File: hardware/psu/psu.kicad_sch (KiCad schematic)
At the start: 58 parts, among them J1 Conn_01x02, J10 Conn_01x04, J11 Conn_01x03, J12 Conn_01x02, J13 Conn_01x03, J14 Conn_01x05, J2 Conn_01x05, J3 Conn_01x02, J4 Conn_01x06, J5 Conn_01x03, J6 Conn_01x05, J7 Conn_01x08, J8 Conn_01x03, J9 Conn_01x04, SW1 SW_SPST, T1 AS-1T175, U1 LM7905_TO220

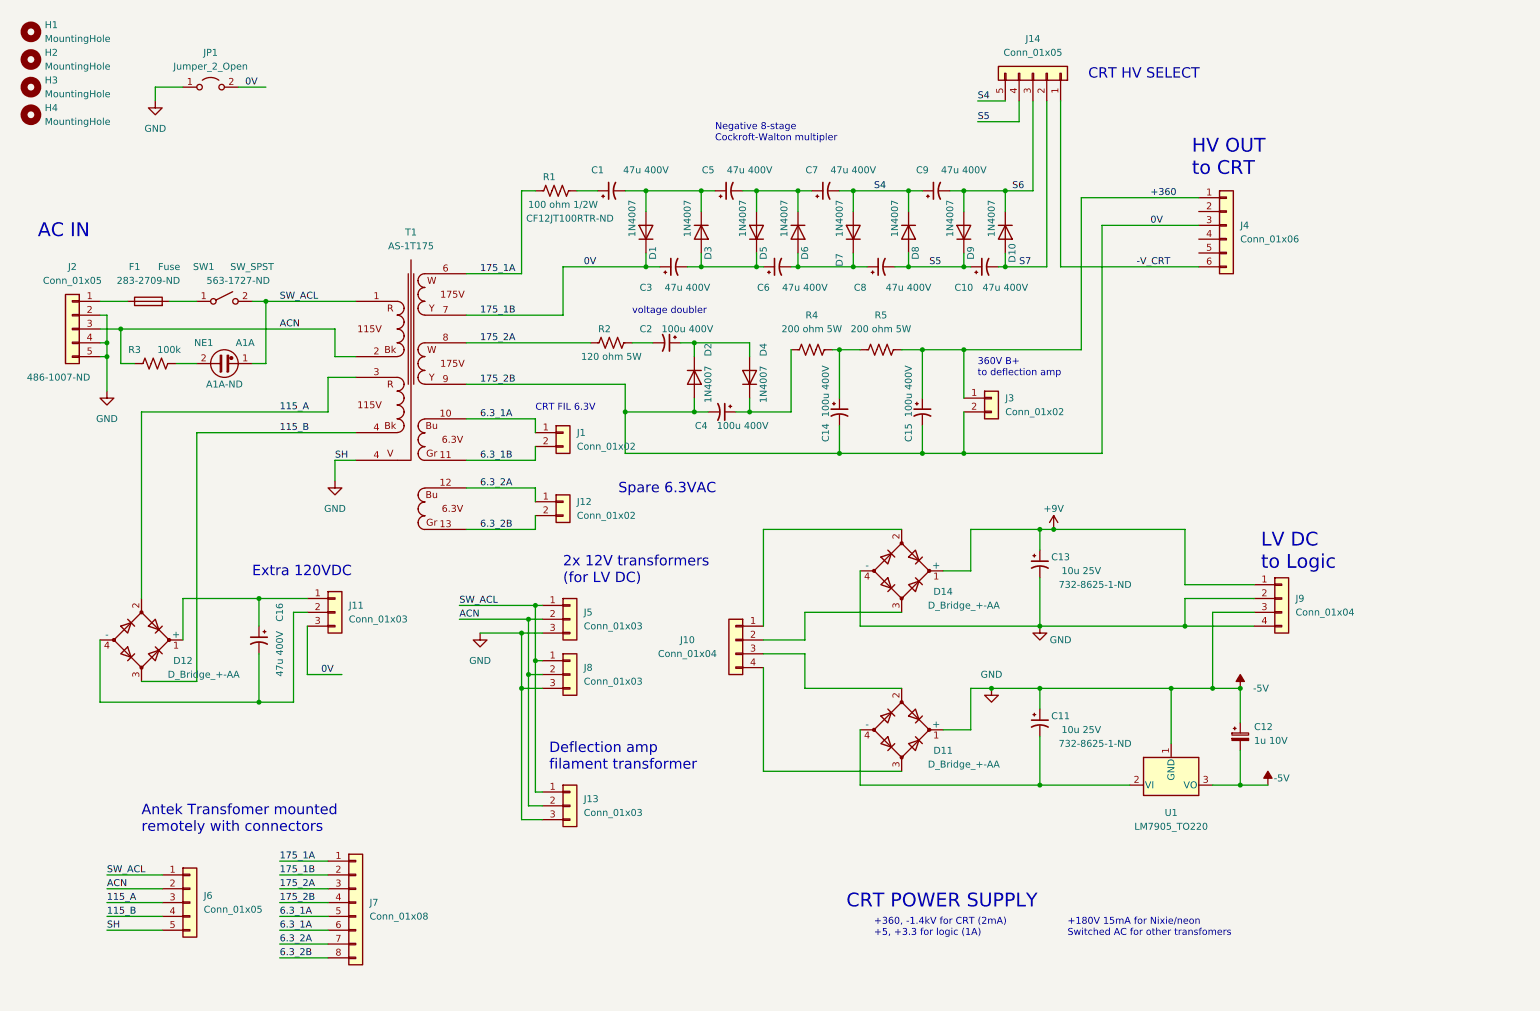
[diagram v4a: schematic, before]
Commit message: Mess with 3D model, clean schematic ERC errors
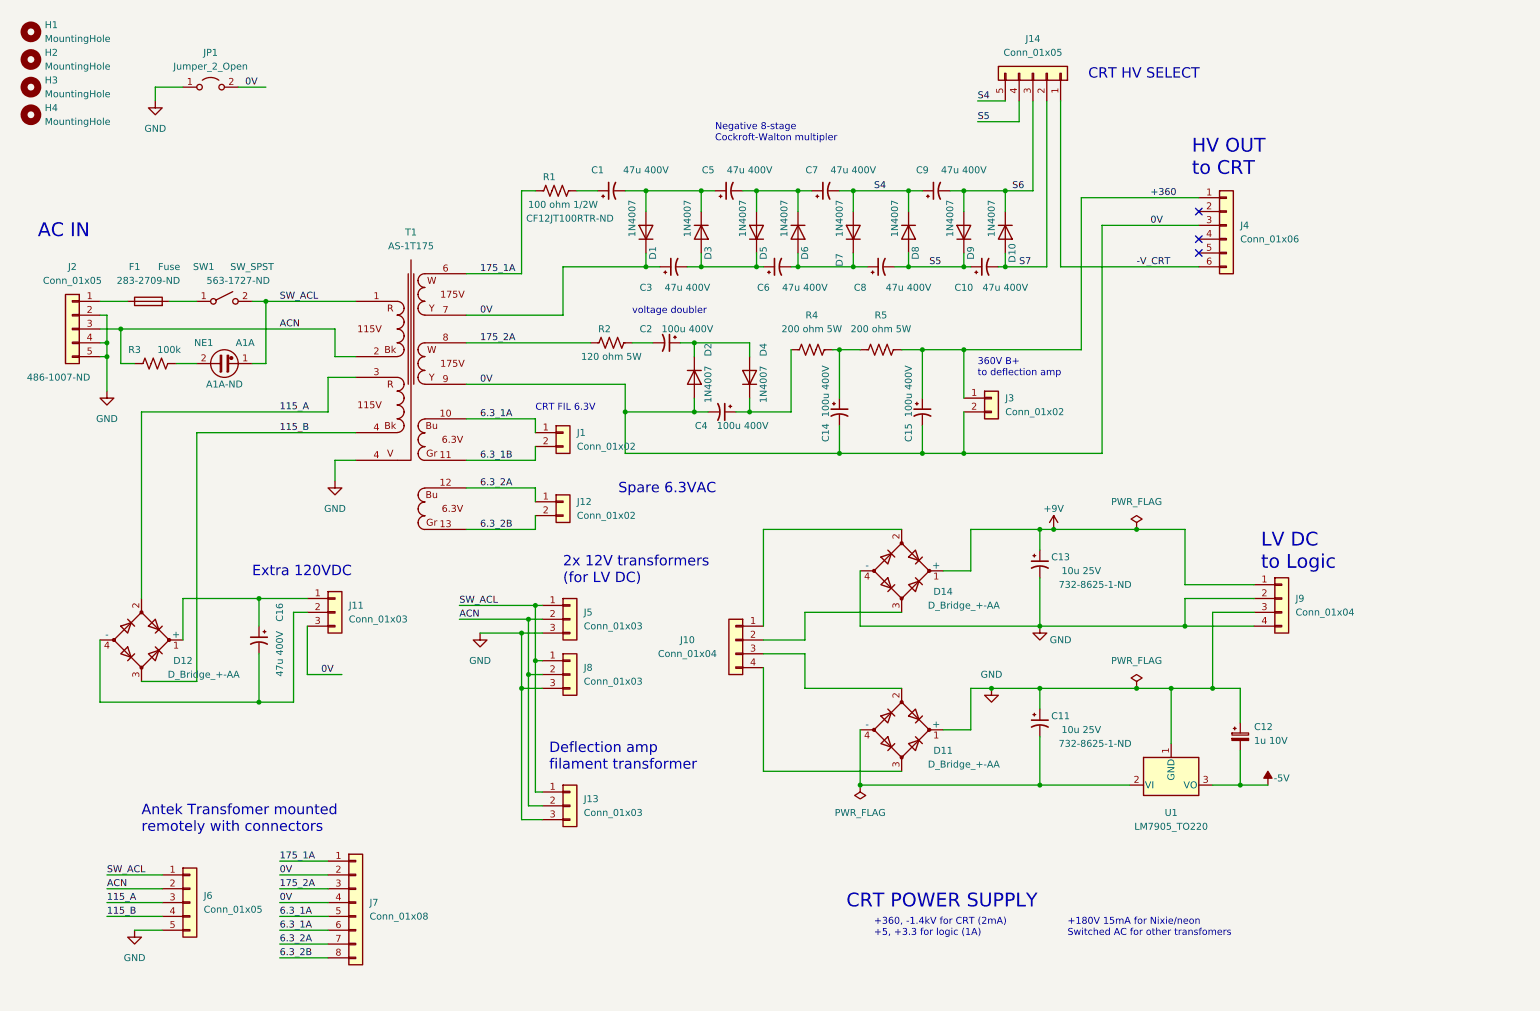
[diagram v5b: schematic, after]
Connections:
- net -5V: no longer C11.1, C12.1, C13.2, D11.1 (+), D14.4 (-), J13.3 (Pin_3), J2.2 (Pin_2), J2.4 (Pin_4), J2.5 (Pin_5), J5.3 (Pin_3), J6.5 (Pin_5), J8.3 (Pin_3), J9.2 (Pin_2), J9.3 (Pin_3), J9.4 (Pin_4), JP1.1 (A), T1.4 (SH), U1.1 (GND)
- new net GND: C11.1, C12.1, C13.2, D11.1 (+), D14.4 (-), J13.3 (Pin_3), J2.2 (Pin_2), J2.4 (Pin_4), J2.5 (Pin_5), J5.3 (Pin_3), J6.5 (Pin_5), J8.3 (Pin_3), J9.2 (Pin_2), J9.3 (Pin_3), J9.4 (Pin_4), JP1.1 (A), T1.4 (SH), U1.1 (GND)
- no-connect marks 0 -> 3
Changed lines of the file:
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@@
   (junction (at 138.43 45.72) (diameter 0) (color 0 0 0 0)
   )
-  (junction (at 237.49 137.16) (diameter 0) (color 0 0 0 0)
-  )
   (junction (at 107.95 132.08) (diameter 0) (color 0 0 0 0)
   )
@@
   (junction (at 200.66 137.16) (diameter 0) (color 0 0 0 0)
   )
+  (junction (at 218.44 137.16) (diameter 0) (color 0 0 0 0)
+  )
   (junction (at 58.42 66.04) (diameter 0) (color 0 0 0 0)
   )
@@
   (junction (at 232.41 137.16) (diameter 0) (color 0 0 0 0)
   )
+  (junction (at 167.64 154.94) (diameter 0) (color 0 0 0 0)
+  )
   (junction (at 200.66 125.73) (diameter 0) (color 0 0 0 0)
   )
@@
   (junction (at 156.21 45.72) (diameter 0) (color 0 0 0 0)
   )
+  (junction (at 218.44 107.95) (diameter 0) (color 0 0 0 0)
+  )
   (junction (at 166.37 59.69) (diameter 0) (color 0 0 0 0)
   )
@@
   (junction (at 105.41 127) (diameter 0) (color 0 0 0 0)
   )
+  (no_connect (at 229.87 57.15))
+  (no_connect (at 229.87 54.61))
+  (no_connect (at 229.87 49.53))
   (wire (pts (xy 200.66 107.95) (xy 203.2 107.95))
     (stroke (width 0) (type default) (color 0 0 0 0))
@@
     (stroke (width 0) (type default) (color 0 0 0 0))
   )
+  (wire (pts (xy 218.44 107.95) (xy 203.2 107.95))
+    (stroke (width 0) (type default) (color 0 0 0 0))
+  )
   (wire (pts (xy 95.25 68.58) (xy 113.03 68.58))
     (stroke (width 0) (type default) (color 0 0 0 0))
@@
     (stroke (width 0) (type default) (color 0 0 0 0))
   )
-  (wire (pts (xy 227.33 107.95) (xy 203.2 107.95))
+  (wire (pts (xy 227.33 107.95) (xy 218.44 107.95))
     (stroke (width 0) (type default) (color 0 0 0 0))
   )
@@
     (stroke (width 0) (type default) (color 0 0 0 0))
   )
-  (wire (pts (xy 200.66 137.16) (xy 224.79 137.16))
+  (wire (pts (xy 200.66 137.16) (xy 218.44 137.16))
     (stroke (width 0) (type default) (color 0 0 0 0))
   )
@@
     (stroke (width 0) (type default) (color 0 0 0 0))
   )
+  (wire (pts (xy 218.44 137.16) (xy 224.79 137.16))
+    (stroke (width 0) (type default) (color 0 0 0 0))
+  )
   (wire (pts (xy 186.69 74.93) (xy 208.28 74.93))
     (stroke (width 0) (type default) (color 0 0 0 0))
@@
     (stroke (width 0) (type default) (color 0 0 0 0))
   )
-  (wire (pts (xy 29.21 181.61) (xy 39.37 181.61))
-    (stroke (width 0) (type default) (color 0 0 0 0))
-  )
   (wire (pts (xy 95.25 95.25) (xy 107.95 95.25))
     (stroke (width 0) (type default) (color 0 0 0 0))
@@
   )
   (wire (pts (xy 106.68 134.62) (xy 106.68 124.46))
+    (stroke (width 0) (type default) (color 0 0 0 0))
+  )
+  (wire (pts (xy 34.29 181.61) (xy 39.37 181.61))
     (stroke (width 0) (type default) (color 0 0 0 0))
   )
@@
     (effects (font (size 1.27 1.27)) (justify left bottom))
   )
-  (label "SH" (at 71.12 95.25 0)
-    (effects (font (size 1.27 1.27)) (justify left bottom))
-  )
   (label "6.3_1B" (at 97.79 95.25 0)
     (effects (font (size 1.27 1.27)) (justify left bottom))
@@
     (effects (font (size 1.27 1.27)) (justify left bottom))
   )
-  (label "175_1B" (at 60.96 171.45 0)
+  (label "0V" (at 60.96 171.45 0)
     (effects (font (size 1.27 1.27)) (justify left bottom))
   )
@@
     (effects (font (size 1.27 1.27)) (justify left bottom))
   )
+  (label "0V" (at 97.79 81.28 0)
+    (effects (font (size 1.27 1.27)) (justify left bottom))
+  )
   (label "115_A" (at 60.96 86.36 0)
     (effects (font (size 1.27 1.27)) (justify left bottom))
   )
-  (label "175_2B" (at 97.79 81.28 0)
-    (effects (font (size 1.27 1.27)) (justify left bottom))
-  )
   (label "0V" (at 220.98 52.07 0)
     (effects (font (size 1.27 1.27)) (justify left bottom))
@@
     (effects (font (size 1.27 1.27)) (justify left bottom))
   )
-  (label "SH" (at 29.21 181.61 0)
-    (effects (font (size 1.27 1.27)) (justify left bottom))
-  )
   (label "115_A" (at 29.21 176.53 0)
     (effects (font (size 1.27 1.27)) (justify left bottom))
   )
-  (label "175_1B" (at 97.79 68.58 0)
-    (effects (font (size 1.27 1.27)) (justify left bottom))
-  )
   (label "S4" (at 170.18 45.72 0)
     (effects (font (size 1.27 1.27)) (justify left bottom))
@@
     (effects (font (size 1.27 1.27)) (justify left bottom))
   )
-  (label "175_2B" (at 60.96 176.53 0)
+  (label "0V" (at 60.96 176.53 0)
     (effects (font (size 1.27 1.27)) (justify left bottom))
   )
@@
     (effects (font (size 1.27 1.27)) (justify left bottom))
   )
-  (label "0V" (at 116.84 59.69 0)
+  (label "0V" (at 97.79 68.58 0)
     (effects (font (size 1.27 1.27)) (justify left bottom))
   )
@@
     (pin "1")
   )
-  (symbol (lib_id "power:-5V") (at 237.49 137.16 0) (unit 1)
-    (in_bom yes) (on_board yes)
-    (property "Reference" "#PWR08" (id 0) (at 237.49 134.62 0)
-      (effects (font (size 1.27 1.27)) hide)
-    )
-    (property "Value" "-5V" (id 1) (at 241.3 137.16 0))
-    (property "Footprint" "" (id 2) (at 237.49 137.16 0)
-      (effects (font (size 1.27 1.27)) hide)
-    )
-    (property "Datasheet" "" (id 3) (at 237.49 137.16 0)
-      (effects (font (size 1.27 1.27)) hide)
-    )
-    (pin "1")
-  )
   (symbol (lib_id "Device:D_Bridge_+AA-") (at 175.26 144.78 0) (unit 1)
     (in_bom yes) (on_board yes)
@@
     (pin "3")
     (pin "4")
+  )
+  (symbol (lib_id "power:PWR_FLAG") (at 218.44 107.95 0) (unit 1)
+    (in_bom yes) (on_board yes) (fields_autoplaced)
+    (property "Reference" "#FLG0102" (id 0) (at 218.44 106.045 0)
+      (effects (font (size 1.27 1.27)) hide)
+    )
+    (property "Value" "PWR_FLAG" (id 1) (at 218.44 102.87 0))
+    (property "Footprint" "" (id 2) (at 218.44 107.95 0)
+      (effects (font (size 1.27 1.27)) hide)
+    )
+    (property "Datasheet" "~" (id 3) (at 218.44 107.95 0)
+      (effects (font (size 1.27 1.27)) hide)
+    )
+    (pin "1")
   )
   (symbol (lib_id "Connector_Generic:Conn_01x03") (at 114.3 134.62 0) (unit 1)
@@
     (pin "1")
   )
+  (symbol (lib_id "power:PWR_FLAG") (at 167.64 154.94 180) (unit 1)
+    (in_bom yes) (on_board yes) (fields_autoplaced)
+    (property "Reference" "#FLG0101" (id 0) (at 167.64 156.845 0)
+      (effects (font (size 1.27 1.27)) hide)
+    )
+    (property "Value" "PWR_FLAG" (id 1) (at 167.64 160.02 0))
+    (property "Footprint" "" (id 2) (at 167.64 154.94 0)
+      (effects (font (size 1.27 1.27)) hide)
+    )
+    (property "Datasheet" "~" (id 3) (at 167.64 154.94 0)
+      (effects (font (size 1.27 1.27)) hide)
+    )
+    (pin "1")
+  )
   (symbol (lib_id "Mechanical:MountingHole") (at 15.24 21.59 0) (unit 1)
     (in_bom yes) (on_board yes) (fields_autoplaced)
@@
     (pin "2")
   )
+  (symbol (lib_id "power:GND") (at 34.29 181.61 0) (unit 1)
+    (in_bom yes) (on_board yes) (fields_autoplaced)
+    (property "Reference" "#PWR0101" (id 0) (at 34.29 187.96 0)
+      (effects (font (size 1.27 1.27)) hide)
+    )
+    (property "Value" "GND" (id 1) (at 34.29 186.69 0))
+    (property "Footprint" "" (id 2) (at 34.29 181.61 0)
+      (effects (font (size 1.27 1.27)) hide)
+    )
+    (property "Datasheet" "" (id 3) (at 34.29 181.61 0)
+      (effects (font (size 1.27 1.27)) hide)
+    )
+    (pin "1")
+  )
   (symbol (lib_id "Device:C_Polarized_Small_US") (at 133.35 59.69 90) (unit 1)
     (in_bom yes) (on_board yes)
@@
     (pin "2")
   )
+  (symbol (lib_id "power:PWR_FLAG") (at 218.44 137.16 0) (unit 1)
+    (in_bom yes) (on_board yes) (fields_autoplaced)
+    (property "Reference" "#FLG0103" (id 0) (at 218.44 135.255 0)
+      (effects (font (size 1.27 1.27)) hide)
+    )
+    (property "Value" "PWR_FLAG" (id 1) (at 218.44 132.08 0))
+    (property "Footprint" "" (id 2) (at 218.44 137.16 0)
+      (effects (font (size 1.27 1.27)) hide)
+    )
+    (property "Datasheet" "~" (id 3) (at 218.44 137.16 0)
+      (effects (font (size 1.27 1.27)) hide)
+    )
+    (pin "1")
+  )
   (symbol (lib_id "Connector_Generic:Conn_01x05") (at 22.86 71.12 0) (mirror y) (unit 1)
     (in_bom yes) (on_board yes)
@@
   )
   (symbol_instances
+    (path "/7c0b2a49-6be3-4836-a134-d8bdbe2029f9"
+      (reference "#FLG0101") (unit 1) (value "PWR_FLAG") (footprint "")
+    )
+    (path "/6ed3655f-29bb-4a2c-8d53-7428c9d0c253"
+      (reference "#FLG0102") (unit 1) (value "PWR_FLAG") (footprint "")
+    )
+    (path "/e589d2a9-ad10-4803-b8dd-58cae92a0830"
+      (reference "#FLG0103") (unit 1) (value "PWR_FLAG") (footprint "")
+    )
     (path "/441877be-212e-4074-8b8d-3abad024027d"
       (reference "#PWR01") (unit 1) (value "GND") (footprint "")
@@
       (reference "#PWR07") (unit 1) (value "+9V") (footprint "")
     )
-    (path "/374684e0-799b-470a-97c1-5ced756bc232"
-      (reference "#PWR08") (unit 1) (value "-5V") (footprint "")
-    )
     (path "/77c041aa-5845-4c96-9371-bd0f80924889"
       (reference "#PWR09") (unit 1) (value "-5V") (footprint "")
     )
+    (path "/8ead9981-91bb-4421-96ed-723a403729f1"
+      (reference "#PWR0101") (unit 1) (value "GND") (footprint "")
+    )
     (path "/59ac5de6-0fe9-487e-9a5e-3c9d13998e39"

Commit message: working on PSU
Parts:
- added J15: Conn_01x02, Connector_PinHeader_2.54mm:PinHeader_1x02_P2.54mm_Vertical, symbol Connector_Generic:Conn_01x02
- added K1: PR16-12V-540-2C, Package_DIP:DIP-22_W7.62mm_LongPads, symbol my_relay:PR16-12V-540-2A
- added Q1: Q_NMOS_GDS, Package_TO_SOT_THT:TO-220-3_Vertical, symbol Device:Q_NMOS_GDS
- added R10, R11, R6, R7, R8, R9: 1.0M 2W, Resistor_THT:R_Axial_DIN0309_L9.0mm_D3.2mm_P15.24mm_Horizontal, symbol Device:R_US
- added U2, U3: BOM_item, symbol misc_bom:BOM_item
- C1, C10, C16, C3, C5, C6, C7, C8, C9: footprint Capacitor_THT:CP_Radial_D13.0mm_P7.50mm -> Capacitor_THT:CP_Radial_D12.5mm_P5.00mm; CatNo (none) -> 565-EKXJ401ELL470MK30S-ND
- C12: footprint Capacitor_THT:CP_Radial_D5.0mm_P2.00mm -> Capacitor_THT:C_Disc_D5.0mm_W2.5mm_P5.00mm; CatNo (none) -> 445-FK28X5R1A105K-ND
- C14, C15, C2, C4: CatNo (none) -> 493-2567-ND
- JP1: value Jumper_2_Open -> WIRE_JUMPER
- R2: footprint Resistor_THT:R_Axial_Power_L25.0mm_W6.4mm_P27.94mm -> Resistor_THT:R_Axial_DIN0617_L17.0mm_D6.0mm_P25.40mm_Horizontal; CatNo (none) -> A142778CT-ND
- R4, R5: footprint Resistor_THT:R_Axial_Power_L25.0mm_W6.4mm_P27.94mm -> Resistor_THT:R_Axial_DIN0617_L17.0mm_D6.0mm_P25.40mm_Horizontal; CatNo (none) -> A142783CT-ND
- U1: CatNo (none) -> LM7905CTNS/NOPB-ND
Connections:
- net 0V: now also R10.1, R11.1, R7.1
- net 175_1A: now also K1.14; no longer T1.6 (H1A)
- net 175_2A: now also K1.9; no longer T1.8 (H2A)
- net GND: now also J15.2 (Pin_2), Q1.3 (S)
- net S7: now also R9.2
- net at C1.2, C5.1, D1.2 (A)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: now also R6.2
- net at C1.1, R1.2: now also R6.1
- net +9V renamed +12V
- net +12V: now also K1.22
- new net: K1.1, Q1.2 (D)
- new net: K1.11, T1.8 (H2A)
- new net: K1.12, T1.6 (H1A)
- new net: K1.16, R11.2
- new net: K1.7, R10.2
- new net: R7.2, R8.1
- new net: J15.1 (Pin_1), Q1.1 (G)
- new net: R8.2, R9.1
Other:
- note added: "(Maybe usable for +5V)"
- note added: "+180V 15mA for Nixie/neon Switched AC for other transformers"
- note added: "5mm 24 pin breakaway header"
- note added: "HV Enable (logic)"
- note added: "Octal Socket"
- note removed: "+180V 15mA for Nixie/neon Switched AC for other transfomers"
- moved on the sheet: C1, C10, C11, C12, C13, C14, C15, C2, C3, C4, C5, C6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

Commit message: PSU layout done?
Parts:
- removed C16: 47u 400V, Capacitor_THT:CP_Radial_D12.5mm_P5.00mm, symbol Device:C_Polarized_Small_US
- removed D12: D_Bridge_+-AA, Diode_THT:Diode_Bridge_19.0x3.5x10.0mm_P5.0mm, symbol Device:D_Bridge_+AA-
- removed J11: Conn_01x03, Connector_Molex:Molex_KK-396_A-41791-0003_1x03_P3.96mm_Vertical, symbol Connector_Generic:Conn_01x03
- removed JP1: WIRE_JUMPER, Connector_PinHeader_2.54mm:PinHeader_1x02_P2.54mm_Vertical, symbol Jumper:Jumper_2_Open
- added R12: 10k, Resistor_THT:R_Axial_DIN0309_L9.0mm_D3.2mm_P12.70mm_Horizontal, symbol Device:R_US
- K1: footprint Package_DIP:DIP-22_W7.62mm_LongPads -> my_relay:DIP-22_W7.62mm_LongPads
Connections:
- net 0V is gone; now on net GND: C14.2, C15.2, C3.1, C4.2, D1.1 (K), D2.2 (A), J3.2 (Pin_2), J4.3 (Pin_3), J7.2 (Pin_2), J7.4 (Pin_4), R10.1, R11.1, R7.1, T1.7 (H1B), T1.9 (H2B)
- net -5V: now also J9.3 (Pin_3)
- net 6.3_1A: no longer J7.6 (Pin_6)
- net 6.3_1B: now also J7.6 (Pin_6)
- net GND: now also R12.1; no longer J9.3 (Pin_3)
- net at D11.2: now also J10.2 (Pin_2); no longer J10.3 (Pin_3)
- net at D11.3: now also J10.1 (Pin_1); no longer J10.4 (Pin_4)
- net at J15.1 (Pin_1), Q1.1 (G): now also R12.2
- net at D14.2: now also J10.4 (Pin_4); no longer J10.1 (Pin_1)
- net at D14.3: now also J10.3 (Pin_3); no longer J10.2 (Pin_2)
- net 115_A: no longer names the net of T1.3 (P2A)
- net 115_A: no longer J6.3 (Pin_3)
- net 115_B: no longer names the net of J6.4 (Pin_4)
- net 115_B: no longer T1.4 (SH)
- no-connect marks 3 -> 7
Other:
- note removed: "Extra 120VDC"
- moved on the sheet: J10, J15
